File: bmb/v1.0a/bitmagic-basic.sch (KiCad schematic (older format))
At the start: 37 parts, among them IC1 CY7C68013A-56, J1 Conn, P1 pkl_USB_OTG, U1 3.3V, U2 USBLC6-2, U3 IP425x-4-TTL, U4 IP425x-4-TTL, U5 24LC00, U6 IP425x-4-TTL, X1 24MHz

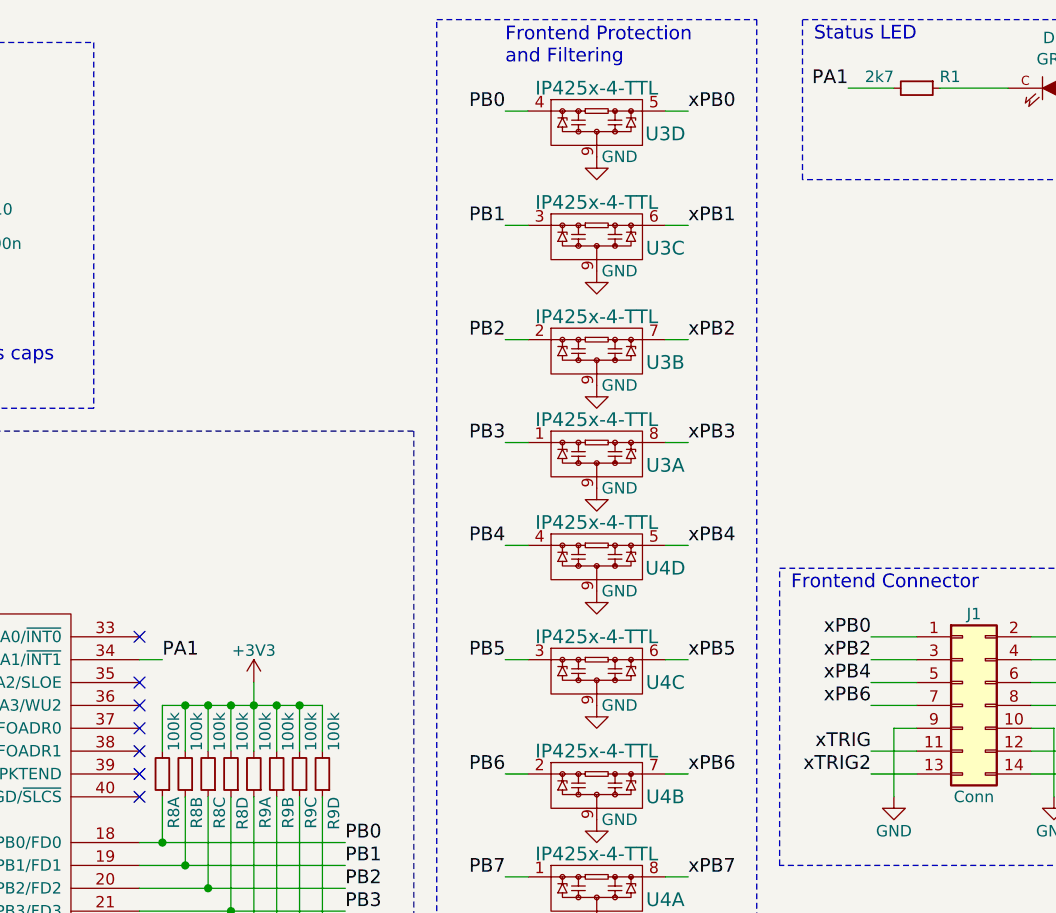
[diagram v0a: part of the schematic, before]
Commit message: Corrected LED and pullup resistor values in V1.0a.
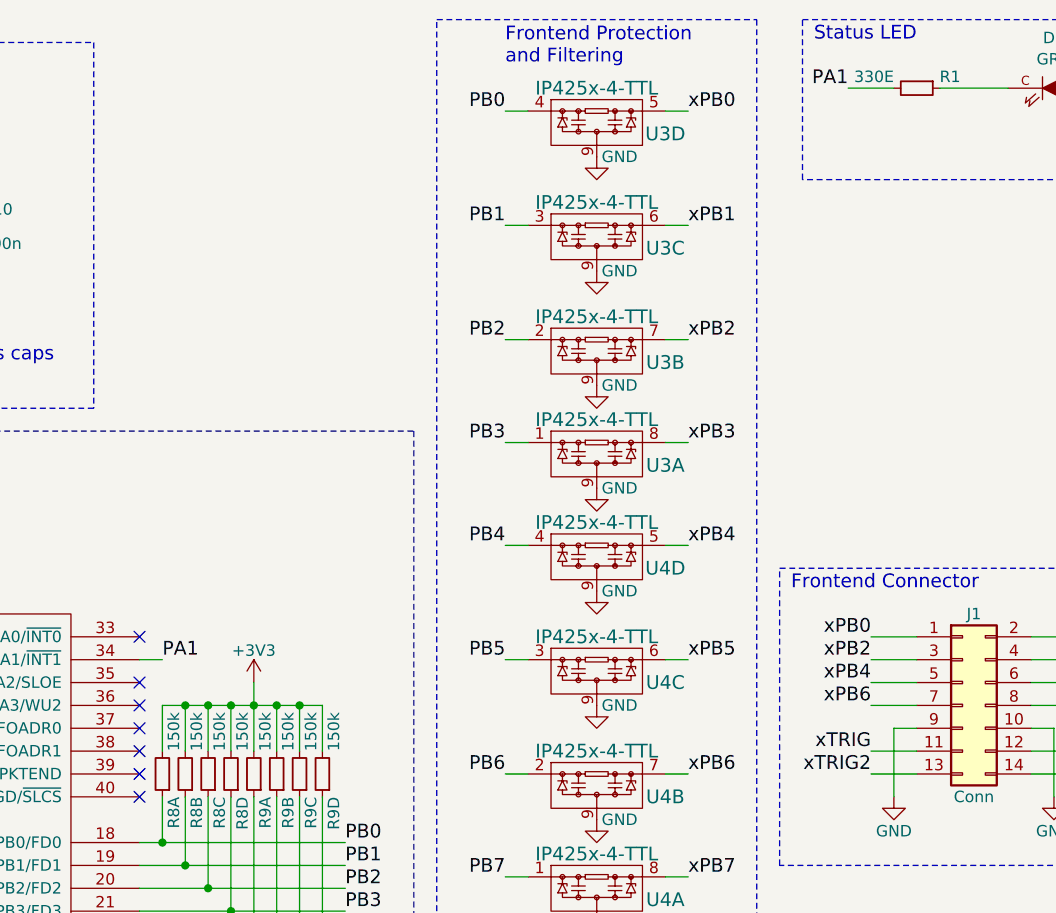
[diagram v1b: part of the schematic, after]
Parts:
- R1: value 2k7 -> 330E; Key res-0402-2k7 -> res-0402-330
- R8, R9: value 100k -> 150k; Key res-0402cv-array-4-100k -> res-0402cv-array-4-150k
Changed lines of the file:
@@
 P 10100 800
 F 0 "R1" V 10050 900 50  0000 L CNN
-F 1 "2k7" V 10050 700 50  0000 R CNN
+F 1 "330E" V 10050 700 50  0000 R CNN
 F 2 "pkl_dipol:R_0402" H 10100 800 60  0001 C CNN
 F 3 "" H 10100 800 60  0000 C CNN
-F 4 "res-0402-2k7" H 10100 800 60  0001 C CNN "Key"
+F 4 "res-0402-330" H 10100 800 60  0001 C CNN "Key"
 F 5 "ANY" H 10100 800 60  0001 C CNN "Source"
 	1    10100 800
@@
 P 6800 3800
 F 0 "R8" V 6750 3900 50  0000 L CNN
-F 1 "100k" V 6750 3700 50  0000 R CNN
+F 1 "150k" V 6750 3700 50  0000 R CNN
 F 2 "pkl_dipol:R_Array_Convex_4x0402" H 6800 3800 60  0001 C CNN
 F 3 "" H 6800 3800 60  0000 C CNN
-F 4 "res-0402cv-array-4-100k" H 6800 3800 60  0001 C CNN "Key"
+F 4 "res-0402cv-array-4-150k" H 6800 3800 60  0001 C CNN "Key"
 F 5 "ANY" H 6800 3800 60  0001 C CNN "Source"
 	1    6800 3800
@@
 P 6900 3800
 F 0 "R8" V 6850 3900 50  0000 L CNN
-F 1 "100k" V 6850 3700 50  0000 R CNN
+F 1 "150k" V 6850 3700 50  0000 R CNN
 F 2 "pkl_dipol:R_Array_Convex_4x0402" H 6900 3800 60  0001 C CNN
 F 3 "" H 6900 3800 60  0000 C CNN
-F 4 "res-0402cv-array-4-100k" H 6900 3800 60  0001 C CNN "Key"
+F 4 "res-0402cv-array-4-150k" H 6900 3800 60  0001 C CNN "Key"
 F 5 "ANY" H 6900 3800 60  0001 C CNN "Source"
 	2    6900 3800
@@
 P 7000 3800
 F 0 "R8" V 6950 3900 50  0000 L CNN
-F 1 "100k" V 6950 3700 50  0000 R CNN
+F 1 "150k" V 6950 3700 50  0000 R CNN
 F 2 "pkl_dipol:R_Array_Convex_4x0402" H 7000 3800 60  0001 C CNN
 F 3 "" H 7000 3800 60  0000 C CNN
-F 4 "res-0402cv-array-4-100k" H 7000 3800 60  0001 C CNN "Key"
+F 4 "res-0402cv-array-4-150k" H 7000 3800 60  0001 C CNN "Key"
 F 5 "ANY" H 7000 3800 60  0001 C CNN "Source"
 	3    7000 3800
@@
 P 7100 3800
 F 0 "R8" V 7050 3900 50  0000 L CNN
-F 1 "100k" V 7050 3700 50  0000 R CNN
+F 1 "150k" V 7050 3700 50  0000 R CNN
 F 2 "pkl_dipol:R_Array_Convex_4x0402" H 7100 3800 60  0001 C CNN
 F 3 "" H 7100 3800 60  0000 C CNN
-F 4 "res-0402cv-array-4-100k" H 7100 3800 60  0001 C CNN "Key"
+F 4 "res-0402cv-array-4-150k" H 7100 3800 60  0001 C CNN "Key"
 F 5 "ANY" H 7100 3800 60  0001 C CNN "Source"
 	4    7100 3800
@@
 P 7200 3800
 F 0 "R9" V 7150 3900 50  0000 L CNN
-F 1 "100k" V 7150 3700 50  0000 R CNN
+F 1 "150k" V 7150 3700 50  0000 R CNN
 F 2 "pkl_dipol:R_Array_Convex_4x0402" H 7200 3800 60  0001 C CNN
 F 3 "" H 7200 3800 60  0000 C CNN
-F 4 "res-0402cv-array-4-100k" H 7200 3800 60  0001 C CNN "Key"
+F 4 "res-0402cv-array-4-150k" H 7200 3800 60  0001 C CNN "Key"
 F 5 "ANY" H 7200 3800 60  0001 C CNN "Source"
 	1    7200 3800
@@
 P 7300 3800
 F 0 "R9" V 7250 3900 50  0000 L CNN
-F 1 "100k" V 7250 3700 50  0000 R CNN
+F 1 "150k" V 7250 3700 50  0000 R CNN
 F 2 "pkl_dipol:R_Array_Convex_4x0402" H 7300 3800 60  0001 C CNN
 F 3 "" H 7300 3800 60  0000 C CNN
-F 4 "res-0402cv-array-4-100k" H 7300 3800 60  0001 C CNN "Key"
+F 4 "res-0402cv-array-4-150k" H 7300 3800 60  0001 C CNN "Key"
 F 5 "ANY" H 7300 3800 60  0001 C CNN "Source"
 	2    7300 3800
@@
 P 7400 3800
 F 0 "R9" V 7350 3900 50  0000 L CNN
-F 1 "100k" V 7350 3700 50  0000 R CNN
+F 1 "150k" V 7350 3700 50  0000 R CNN
 F 2 "pkl_dipol:R_Array_Convex_4x0402" H 7400 3800 60  0001 C CNN
 F 3 "" H 7400 3800 60  0000 C CNN
-F 4 "res-0402cv-array-4-100k" H 7400 3800 60  0001 C CNN "Key"
+F 4 "res-0402cv-array-4-150k" H 7400 3800 60  0001 C CNN "Key"
 F 5 "ANY" H 7400 3800 60  0001 C CNN "Source"
 	3    7400 3800
@@
 P 7500 3800
 F 0 "R9" V 7450 3900 50  0000 L CNN
-F 1 "100k" V 7450 3700 50  0000 R CNN
+F 1 "150k" V 7450 3700 50  0000 R CNN
 F 2 "pkl_dipol:R_Array_Convex_4x0402" H 7500 3800 60  0001 C CNN
 F 3 "" H 7500 3800 60  0000 C CNN
-F 4 "res-0402cv-array-4-100k" H 7500 3800 60  0001 C CNN "Key"
+F 4 "res-0402cv-array-4-150k" H 7500 3800 60  0001 C CNN "Key"
 F 5 "ANY" H 7500 3800 60  0001 C CNN "Source"
 	4    7500 3800
